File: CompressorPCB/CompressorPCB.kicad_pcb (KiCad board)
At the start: 4 copper layers, 118 parts, among them J1 PowerJack, J2 SWD Header, J3 Header, J5 In, J6 Out, Q1 BC847, Q2 BC857, Q3 BC857, Q4 2N7002, SW2 RST, U1 TL074, U2 TL074, U3 LM13700, U4 LMR62014XMF, U5 AMS1117, U6 NCS20074D, U7 STM32L052K6T6, U8 74HC595, U9 74HC595

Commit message: fixed resistor array footprints
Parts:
- removed RN3, RN4: 470, Resistor_THT:R_Array_SIP8
- added RN5: 470, Resistor_SMD:R_Cat16-4, F.Cu at (209.5, -3.92)
- added RN6: 470, Resistor_SMD:R_Cat16-4, F.Cu at (213.4, -3.92)
- RN1, RN2: footprint Resistor_THT:R_Array_SIP8 -> Resistor_SMD:R_Cat16-4
- moved RN1 75.9 mm to (166.9, -24.8)
- moved U10 71.0 mm to (174.0, -43.9)
- moved RN2 46.7 mm to (205.7, -3.92)
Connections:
- RN1 pad 2: GND -> Net-(RN1B-R2.1)
- RN1 pad 3: Net-(RN1B-R2.1) -> Net-(RN1C-R3.1)
- RN1 pad 4: GND -> Net-(RN1D-R4.1)
- RN1 pad 5: Net-(RN1C-R3.1) -> GND
- RN1 pad 7: Net-(RN1D-R4.1) -> GND
- RN2 pad 2: GND -> Net-(RN2B-R2.1)
- RN2 pad 3: Net-(RN2B-R2.1) -> Net-(RN2C-R3.1)
- RN2 pad 4: GND -> Net-(RN2D-R4.1)
- RN2 pad 5: Net-(RN2C-R3.1) -> GND
- RN2 pad 7: Net-(RN2D-R4.1) -> GND
- U10 pad 10: Net-(RN2A-R1.1) -> Net-(RN1A-R1.1)
- U10 pad 12: Net-(RN2B-R2.1) -> Net-(RN1B-R2.1)
- U10 pad 14: Net-(RN2C-R3.1) -> Net-(RN1C-R3.1)
- U10 pad 16: Net-(RN2D-R4.1) -> Net-(RN1D-R4.1)
- U10 pad 2: Net-(RN1A-R1.1) -> Net-(RN5A-R1.1)
- U10 pad 4: Net-(RN1B-R2.1) -> Net-(RN5B-R2.1)
- U10 pad 6: Net-(RN1C-R3.1) -> Net-(RN5C-R3.1)
- U10 pad 8: Net-(RN1D-R4.1) -> Net-(RN5D-R4.1)
- U11 pad 10: Net-(RN4A-R1.1) -> Net-(RN2A-R1.1)
- U11 pad 12: Net-(RN4B-R2.1) -> Net-(RN2B-R2.1)
- U11 pad 14: Net-(RN4C-R3.1) -> Net-(RN2C-R3.1)
- U11 pad 16: Net-(RN4D-R4.1) -> Net-(RN2D-R4.1)

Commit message: basic layout
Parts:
- C1, C10, C11, C12, C13, C14, C15, C16, C17, C18, C19, C2, C20, C22, C3, C4, C5, C6, C7, C8, C9, D1, D10, D12, D13, D14, D15, D16, D2, D6, D9, J1, J2, J5, J6, J8, L1, Q1, Q2, Q3, Q4, R1, R11, R12, R13, R14, R15, R16, R17, R18, R19, R2, R20, R21, R22, R23, R24, R26, R27, R29, R3, R30, R31, R33, R34, R35, R36, R37, R38, R39, R4, R40, R41, R42, R43, R44, R45, R46, R47, R48, R49, R5, R50, R51, R52, R53, R54, R56, R57, R7, R8, R9, SW2, U1, U2, U3, U4, U5, U6, U7: moved to B.Cu
- moved R28 331.9 mm to (-39.0, 33.2)
- moved R32 315.9 mm to (-4.75, 30.4)
- moved R41 307.9 mm to (-20.4, -2.23), turned to 180 degrees
- moved D15 307.8 mm to (-38.5, 24.1), turned to -90 degrees
- moved SW2 306.8 mm to (-39.6, 15.1), turned to -90 degrees
- moved D14 304.4 mm to (-31.6, 29.3), turned to 180 degrees
- moved J2 300.5 mm to (-40.5, -42.7), turned to 180 degrees
- moved D16 297.4 mm to (-31.6, 15.7)
- moved C15 296.7 mm to (-16.3, -2.23)
- moved D12 290.3 mm to (-23.7, 3.48), turned to 180 degrees
- moved D13 287.7 mm to (-20.8, 7.38), turned to 90 degrees
- moved C1 285.0 mm to (-33.0, 21.8)
- moved U1 284.3 mm to (-27.3, 21.8)
- moved U7 282.9 mm to (-18.7, -17.4), turned to -135 degrees
- moved Q1 282.5 mm to (-9.60, 5.57), turned to 180 degrees
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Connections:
- C2 pad 2: Net-(U1A-+) -> Net-(U1D-+)
- R1 pad 1: Net-(U1A-+) -> Net-(U1D-+)
- R12 pad 2: Net-(U1B--) -> Net-(U1A--)
- R16 pad 1: Net-(U1B--) -> Net-(U1A--)
- R17 pad 1: Net-(U1B--) -> Net-(U1A--)
- R19 pad 2: Net-(U1C--) -> Net-(U1B--)
- R2 pad 1: Net-(U2B--) -> Net-(U2C--)
- R23 pad 1: Net-(U1C--) -> Net-(U1B--)
- R25 pad 2: Net-(U2A-+) -> Net-(U2B-+)
- R29 pad 2: Net-(U2A--) -> Net-(U2B--)
- R3 pad 1: Net-(U2B--) -> Net-(U2C--)
- R31 pad 1: Net-(U2A--) -> Net-(U2B--)
- R4 pad 1: Net-(U1A--) -> Net-(U1D--)
- R44 pad 2: Net-(U6C--) -> Net-(U6D--)
- R46 pad 1: Net-(U6C--) -> Net-(U6D--)
- R49 pad 2: Net-(U6D--) -> Net-(U6C--)
- R5 pad 1: Net-(U1A--) -> Net-(U1D--)
- R50 pad 1: Net-(U6D--) -> Net-(U6C--)
- RN1 pad 1: Net-(RN1A-R1.1) -> GND
- RN1 pad 2: Net-(RN1B-R2.1) -> GND
- RN1 pad 3: Net-(RN1C-R3.1) -> GND
- RN1 pad 4: Net-(RN1D-R4.1) -> GND
- RN1 pad 5: GND -> Net-(RN1D-R4.2)
- RN1 pad 6: GND -> Net-(RN1C-R3.2)
- RN1 pad 7: GND -> Net-(RN1B-R2.2)
- RN1 pad 8: GND -> Net-(RN1A-R1.2)
- RN2 pad 1: Net-(RN2A-R1.1) -> GND
- RN2 pad 2: Net-(RN2B-R2.1) -> GND
- RN2 pad 3: Net-(RN2C-R3.1) -> GND
- RN2 pad 4: Net-(RN2D-R4.1) -> GND
- RN2 pad 5: GND -> Net-(RN2D-R4.2)
- RN2 pad 6: GND -> Net-(RN2C-R3.2)
- RN2 pad 7: GND -> Net-(RN2B-R2.2)
- RN2 pad 8: GND -> Net-(RN2A-R1.2)
- RN5 pad 1: Net-(RN5A-R1.1) -> GND
- RN5 pad 2: Net-(RN5B-R2.1) -> GND
- RN5 pad 3: Net-(RN5C-R3.1) -> GND
- RN5 pad 4: Net-(RN5D-R4.1) -> GND
- RN5 pad 5: GND -> Net-(RN5D-R4.2)
- RN5 pad 6: GND -> Net-(RN5C-R3.2)
- RN5 pad 7: GND -> Net-(RN5B-R2.2)
- RN5 pad 8: GND -> Net-(RN5A-R1.2)
- RN6 pad 1: Net-(RN6A-R1.1) -> GND
- RN6 pad 2: Net-(RN6B-R2.1) -> GND
- RN6 pad 3: Net-(RN6C-R3.1) -> GND
- RN6 pad 4: Net-(RN6D-R4.1) -> GND
- RN6 pad 5: GND -> Net-(RN6D-R4.2)
- RN6 pad 6: GND -> Net-(RN6C-R3.2)
- RN6 pad 7: GND -> Net-(RN6B-R2.2)
- RN6 pad 8: GND -> Net-(RN6A-R1.2)
- U1 pad 1: /Analog/InAmp -> Net-(D14-K)
- U1 pad 10: /Analog/Dcathode -> /Analog/EnvCap
- U1 pad 12: /Analog/EnvCap -> Net-(U1D-+)
- U1 pad 13: ENV -> Net-(U1D--)
- U1 pad 14: ENV -> /Analog/InAmp
- U1 pad 3: Net-(U1A-+) -> +9VA
- U1 pad 5: +9VA -> /Analog/Dcathode
- U1 pad 7: Net-(D14-K) -> Net-(D16-A)
- U1 pad 8: Net-(D16-A) -> ENV
- U1 pad 9: Net-(U1C--) -> ENV
- U10 pad 10: Net-(RN1A-R1.1) -> Net-(RN1A-R1.2)
- U10 pad 12: Net-(RN1B-R2.1) -> Net-(RN1B-R2.2)
- U10 pad 14: Net-(RN1C-R3.1) -> Net-(RN1C-R3.2)
- U10 pad 16: Net-(RN1D-R4.1) -> Net-(RN1D-R4.2)
- U10 pad 2: Net-(RN5A-R1.1) -> Net-(RN5A-R1.2)
- U10 pad 4: Net-(RN5B-R2.1) -> Net-(RN5B-R2.2)
- U10 pad 6: Net-(RN5C-R3.1) -> Net-(RN5C-R3.2)
- U10 pad 8: Net-(RN5D-R4.1) -> Net-(RN5D-R4.2)
- U11 pad 10: Net-(RN2A-R1.1) -> Net-(RN2A-R1.2)
- U11 pad 12: Net-(RN2B-R2.1) -> Net-(RN2B-R2.2)
- U11 pad 14: Net-(RN2C-R3.1) -> Net-(RN2C-R3.2)
- U11 pad 16: Net-(RN2D-R4.1) -> Net-(RN2D-R4.2)
- U11 pad 2: Net-(RN6A-R1.1) -> Net-(RN6A-R1.2)
- U11 pad 4: Net-(RN6B-R2.1) -> Net-(RN6B-R2.2)
- U11 pad 6: Net-(RN6C-R3.1) -> Net-(RN6C-R3.2)
- U11 pad 8: Net-(RN6D-R4.1) -> Net-(RN6D-R4.2)
- U2 pad 1: Net-(C7-Pad1) -> Net-(Q1-B)
- U2 pad 10: Vamp -> ENV
- U2 pad 2: Net-(U2A--) -> Net-(Q1-E)
- U2 pad 3: Net-(U2A-+) -> Vamp
- U2 pad 5: ENV -> Net-(U2B-+)
- U2 pad 7: /Analog/RatioAmp -> Net-(C7-Pad1)
- U2 pad 8: Net-(Q1-B) -> /Analog/RatioAmp
- U2 pad 9: Net-(Q1-E) -> Net-(U2C--)
- U6 pad 14: Net-(R50-Pad2) -> Net-(R46-Pad2)
- U6 pad 8: Net-(R46-Pad2) -> Net-(R50-Pad2)
- U7 pad 10: /Digital/LED_Latch -> unconnected-(U7-PA4-Pad10)
- U7 pad 11: /Digital/LED_SCK -> unconnected-(U7-PA5-Pad11)
- U7 pad 13: /Digital/LED_MOSI -> unconnected-(U7-PA7-Pad13)
- U7 pad 14: /Digital/LED_NRST -> unconnected-(U7-PB0-Pad14)
- U7 pad 20: unconnected-(U7-PA10-Pad20) -> /Digital/BYP_LED
- U7 pad 25: unconnected-(U7-PA15-Pad25) -> /Digital/LED_Latch
- U7 pad 26: /Digital/BYP_LED -> /Digital/LED_SCK
- U7 pad 28: unconnected-(U7-PB5-Pad28) -> /Digital/LED_MOSI
- U7 pad 29: unconnected-(U7-PB6-Pad29) -> /Digital/LED_NRST
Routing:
- added copper zone on B.Cu, net GND
- added copper zone on F.Cu, net GND
- added copper zone on In1.Cu, net GND
- added copper zone on In2.Cu, net GND

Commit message: routing start
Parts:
- moved R48 3.40 mm to (-11.7, -7.72)
- moved C16 2.13 mm to (-8.32, -7.65)
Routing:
- net +3.3V: track 0.00 -> 233.3 mm, vias 0 -> 3
- net +9VA: track 0.00 -> 170.5 mm, vias 0 -> 3
- net +18V: track 0.00 -> 152.5 mm, vias 0 -> 8
- net NRST: track 0.00 -> 84.9 mm, vias 0 -> 1
- net /Digital/LED_NRST: track 0.00 -> 84.9 mm, vias 0 -> 2
- net /Digital/LED_Latch: track 0.00 -> 77.3 mm, vias 0 -> 2
- net /Digital/LED_SCK: track 0.00 -> 65.8 mm, vias 0 -> 2
- net Net-(U8-QH'): track 0.00 -> 62.4 mm, vias 0 -> 2
- net VCC: track 0.00 -> 51.3 mm
- net Net-(U8-QA): track 0.00 -> 34.4 mm
- net +3.3VA: track 0.00 -> 34.3 mm, vias 0 -> 1
- net SWCLK: track 0.00 -> 31.6 mm
- net SWDIO: track 0.00 -> 28.6 mm
- net /Digital/Output_ADC: track 0.00 -> 24.2 mm, vias 0 -> 2
- net Net-(U8-QB): track 0.00 -> 23.0 mm
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
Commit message: all routed, no DRC
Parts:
- moved R56 10.6 mm to (-11.9, -13.4)
- moved C20 0.17 mm to (-20.6, -7.52)
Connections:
- J3 pad 1: /Digital/InJack -> /Digital/OutJack
- J3 pad 2: FX_IN -> FX_OUT
- J3 pad 3: /Digital/OutJack -> /Digital/InJack
- J3 pad 4: FX_OUT -> FX_IN
- U7 pad 18: BYP_IN -> unconnected-(U7-PA8-Pad18)
- U7 pad 9: unconnected-(U7-PA3-Pad9) -> BYP_IN
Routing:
- net /Digital/OutJack: track 0.00 -> 96.8 mm, vias 0 -> 1
- net BYP_IN: track 2.09 -> 88.0 mm, vias 0 -> 2
- net OUT_BIASED: track 0.00 -> 84.5 mm, vias 0 -> 2
- net Net-(U2B-+): track 0.00 -> 76.6 mm, vias 0 -> 2
- net /Digital/InJack: track 0.00 -> 76.0 mm
- net Net-(D13-K): track 0.00 -> 75.9 mm, vias 0 -> 2
- net ENV: track 1.27 -> 65.7 mm, vias 0 -> 2
- net FX_IN: track 0.00 -> 45.9 mm
- net /Digital/BYP_LED: track 0.00 -> 41.0 mm, vias 0 -> 2
- net Net-(R46-Pad2): track 4.23 -> 44.5 mm, vias 0 -> 2
- net /Analog/EnvCap: track 0.00 -> 40.3 mm, vias 0 -> 1
- net FX_OUT: track 0.00 -> 38.7 mm, vias 0 -> 1
- net /Analog/RatioAmp: track 0.00 -> 32.3 mm, vias 0 -> 2
- net /Digital/LED_SCK: track 65.8 -> 97.5 mm, vias 2 -> 3
- net /Analog/InAmp: track 0.00 -> 28.6 mm, vias 0 -> 2
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
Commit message: niceties
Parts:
- moved SW2 35.9 mm to (-39.1, -20.8)
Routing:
- net NRST: track 84.9 -> 47.3 mm
- net SWCLK: track 31.6 -> 34.3 mm
- net /Digital/OutJack: track 96.8 -> 99.2 mm
- net SWDIO: track 28.6 -> 30.9 mm
- net /Digital/LED_SCK: track 97.5 -> 99.4 mm
- net /Digital/LED_Latch: track 102.4 -> 103.9 mm
- net /Analog/FullRect: track 25.9 -> 24.4 mm
- net /Digital/LED_MOSI: track 24.4 -> 25.5 mm
- net Net-(U9-QA): track 20.7 -> 19.5 mm
- net Net-(U8-QB): track 23.0 -> 21.9 mm
- net Net-(RN1D-R4.2): track 5.21 -> 6.09 mm
- net Net-(R18-Pad1): track 16.3 -> 15.6 mm
- net GND: vias 52 -> 77

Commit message: routing start
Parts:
- removed D14, D15, D2: 1N4148W, Diode_SMD:D_SOD-123
- removed R23, R42: 100k, Resistor_SMD:R_0805_2012Metric
- removed R27, R30: 1k, Resistor_SMD:R_0805_2012Metric
- removed R47: 680k, Resistor_SMD:R_0805_2012Metric
- added C24: 22n, Capacitor_SMD:C_0805_2012Metric, B.Cu at (12.1, -12.7)
- added R58: 220, Resistor_SMD:R_0805_2012Metric, B.Cu at (0.77, -0.42)
- added R59: 100k, Resistor_SMD:R_0805_2012Metric, B.Cu at (-9.76, -5.93)
- added R60: 47k, Resistor_SMD:R_0805_2012Metric, B.Cu at (7.78, -2.33)
- added R61: 22k, Resistor_SMD:R_0805_2012Metric, B.Cu at (5.28, 0.72)
- C16: value 1u -> 470n
- R12: value 100k -> 10k
- R16: value 100k -> 1k
- R19: value 100k -> 220
- R43: value 47k -> 91k
- R44: value 56k -> 47k
- R45: value 22k -> 47k
- R48: value 10k -> 1k
- moved R16 33.9 mm to (-3.91, 34.8), turned to 0 degrees
- moved R12 30.2 mm to (2.76, 33.1)
- moved R44 17.0 mm to (-5.68, -9.47), turned to -90 degrees
- moved R49 14.1 mm to (15.9, -12.4), turned to 90 degrees
- moved D16 12.8 mm to (-35.0, 28.0)
- moved C18 12.6 mm to (8.41, -6.31), turned to 0 degrees
- moved R2 11.9 mm to (-13.0, 20.2)
- moved R46 11.9 mm to (-2.19, -9.62), turned to 90 degrees
- moved R48 7.57 mm to (-6.36, -2.37), turned to -90 degrees
- moved R17 7.47 mm to (-36.2, 20.7), turned to 90 degrees
- moved R54 7.12 mm to (0.33, -17.6)
- moved R43 6.82 mm to (9.76, -9.15), turned to 90 degrees
- moved R19 5.82 mm to (-38.0, 24.0), turned to 0 degrees
- moved C16 5.48 mm to (-9.77, -2.36), turned to 90 degrees
- moved R1 3.90 mm to (-18.1, 24.2)
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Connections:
- D16 pad 1: /Analog/FullRect -> Net-(D16-K)
- R12 pad 1: /Analog/InAmp -> Net-(R12-Pad1)
- R12 pad 2: Net-(U1A--) -> Net-(U1C-+)
- R16 pad 1: Net-(U1A--) -> ENV
- R16 pad 2: /Analog/Dcathode -> Net-(R12-Pad1)
- R17 pad 1: Net-(U1A--) -> /Analog/EnvCap
- R17 pad 2: /Analog/Danode -> Net-(U1C--)
- R19 pad 1: /Analog/Danode -> Net-(D16-K)
- R19 pad 2: Net-(U1B--) -> Net-(U1A--)
- R28 pad 1: Net-(R27-Pad2) -> Net-(U1A--)
- R32 pad 2: Net-(R30-Pad2) -> Net-(U1C-+)
- R32 pad 3: Net-(R30-Pad2) -> Net-(R12-Pad1)
- R49 pad 1: Net-(U6B--) -> Net-(R49-Pad1)
- R49 pad 2: Net-(U6C--) -> Net-(U6A--)
- R50 pad 1: Net-(U6C--) -> Net-(U6A--)
- R50 pad 2: Net-(R50-Pad2) -> Net-(C24-Pad2)
- R54 pad 1: Net-(R50-Pad2) -> Net-(C24-Pad2)
- U1 pad 1: Net-(D14-K) -> Net-(D16-A)
- U1 pad 10: /Analog/EnvCap -> Net-(U1C-+)
- U1 pad 3: +9VA -> /Analog/InAmp
- U1 pad 5: /Analog/Dcathode -> /Analog/EnvCap
- U1 pad 6: Net-(U1B--) -> ENV
- U1 pad 7: Net-(D16-A) -> ENV
- U1 pad 8: ENV -> Net-(U1C--)
- U1 pad 9: ENV -> Net-(U1C--)
- U2 pad 10: ENV -> unconnected-(U2C-+-Pad10)
- U6 pad 1: Net-(D1-A) -> Net-(C24-Pad2)
- U6 pad 10: /Digital/vMirror -> OUT_BIASED
- U6 pad 2: Net-(D2-A) -> Net-(U6A--)
- U6 pad 3: +9VA -> /Digital/vMirror
- U6 pad 7: Net-(U6B--) -> Net-(R49-Pad1)
- U6 pad 8: Net-(R50-Pad2) -> Net-(R58-Pad1)
- U6 pad 9: Net-(U6C--) -> /Digital/Rect
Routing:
- net +3.3V: track 248.6 -> 39.0 mm, vias 3 -> 0
- net /Digital/OutJack: track 99.2 -> 0.00 mm, vias 1 -> 0
- net OUT_BIASED: track 84.5 -> 0.00 mm, vias 2 -> 0
- net BYP_IN: track 88.0 -> 3.55 mm, vias 2 -> 0
- net /Digital/LED_NRST: track 107.8 -> 30.4 mm, vias 2 -> 1
- net Net-(U2B-+): track 76.6 -> 0.00 mm, vias 2 -> 0
- net /Digital/InJack: track 76.0 -> 0.00 mm
- net Net-(D13-K): track 75.9 -> 0.00 mm, vias 2 -> 0
- net /Digital/LED_Latch: track 103.9 -> 29.8 mm, vias 3 -> 1
- net /Digital/LED_SCK: track 99.4 -> 27.2 mm, vias 3 -> 1
- net FX_IN: track 45.9 -> 0.00 mm
- net /Digital/BYP_LED: track 41.0 -> 0.00 mm, vias 2 -> 0
- net FX_OUT: track 38.7 -> 0.00 mm, vias 1 -> 0
- net Net-(R46-Pad2): track 44.5 -> 8.76 mm, vias 2 -> 0
- net NRST: track 47.3 -> 14.3 mm, vias 1 -> 0
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
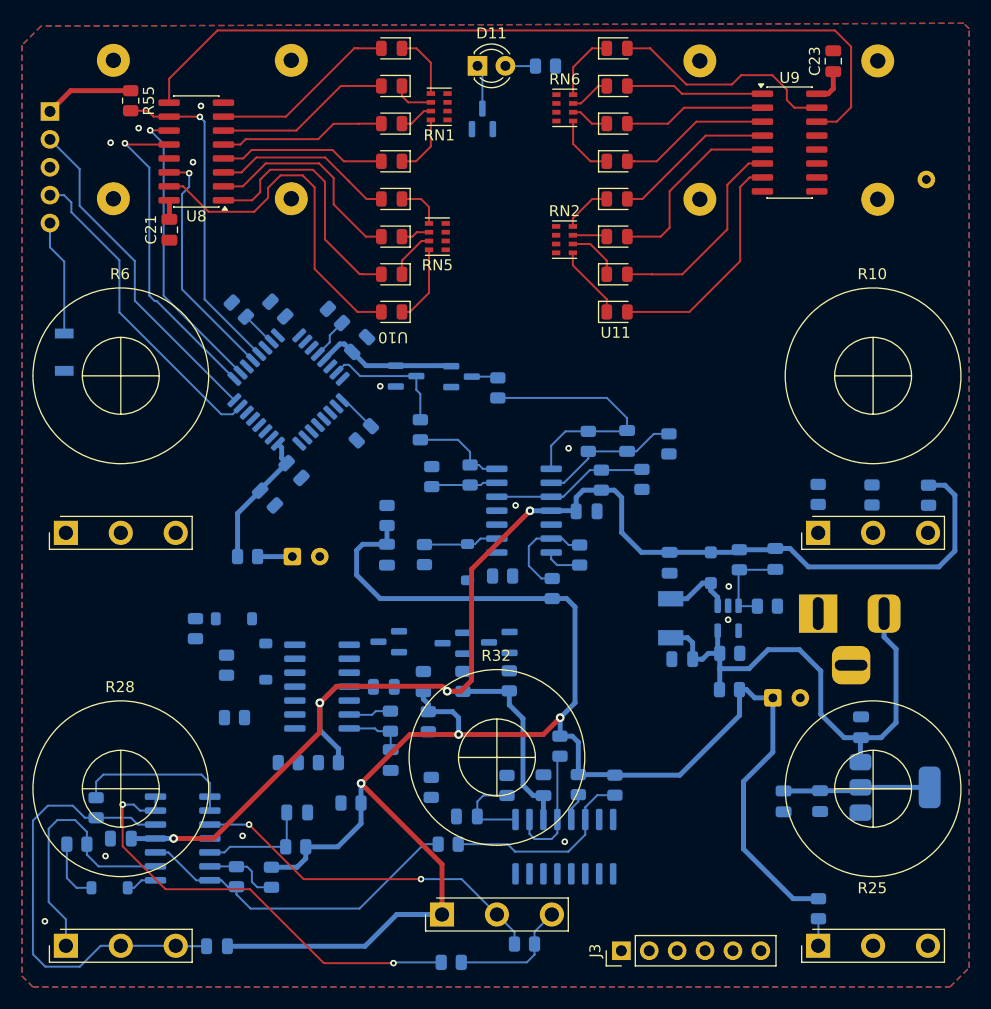
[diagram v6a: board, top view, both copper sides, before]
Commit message: all routed, DRC passing
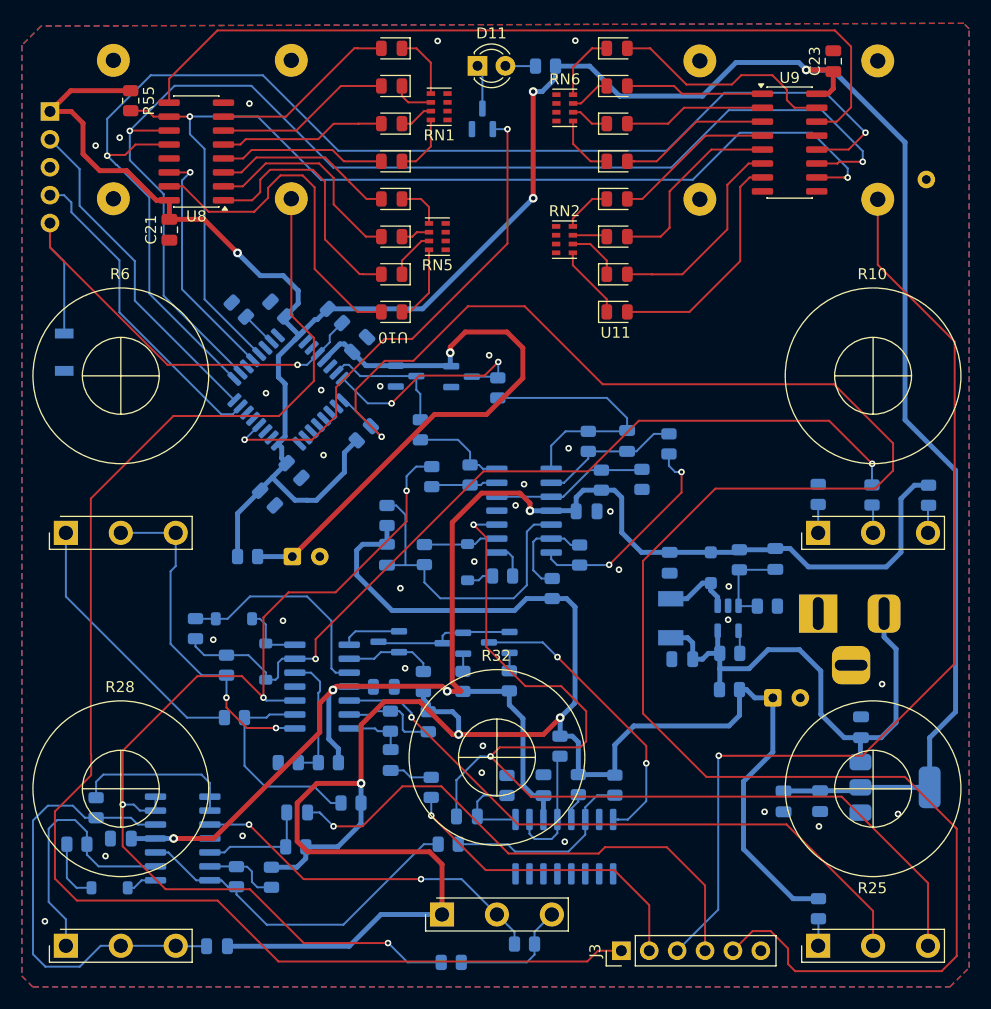
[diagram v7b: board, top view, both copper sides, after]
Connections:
- U2 pad 10: unconnected-(U2C-+-Pad10) -> ENV
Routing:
- net +3.3V: track 39.0 -> 238.6 mm, vias 0 -> 4
- net BYP_IN: track 3.55 -> 178.5 mm, vias 0 -> 1
- net /Digital/OutJack: track 0.00 -> 133.3 mm
- net OUT_BIASED: track 0.00 -> 94.9 mm, vias 0 -> 2
- net /Digital/InJack: track 0.00 -> 89.5 mm, vias 0 -> 1
- net /Digital/LED_Latch: track 29.8 -> 116.9 mm, vias 1 -> 2
- net /Digital/LED_SCK: track 27.2 -> 110.3 mm, vias 1 -> 2
- net Net-(D13-K): track 0.00 -> 79.1 mm, vias 0 -> 2
- net /Digital/LED_NRST: track 30.4 -> 98.9 mm, vias 1 -> 2
- net Net-(U2B-+): track 0.00 -> 59.1 mm, vias 0 -> 1
- net ENV: track 41.7 -> 96.7 mm, vias 2 -> 4
- net FX_IN: track 0.00 -> 48.4 mm, vias 0 -> 1
- net /Digital/BYP_LED: track 0.00 -> 46.5 mm, vias 0 -> 2
- net +3.3VA: track 16.2 -> 56.2 mm, vias 0 -> 1
- net /Analog/RatioAmp: track 0.00 -> 31.6 mm, vias 0 -> 2
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
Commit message: elbow room, stitching vias
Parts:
- moved R12 1.35 mm to (2.77, 34.4)
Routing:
- net +3.3VA: track 56.2 -> 42.0 mm
- net Net-(R49-Pad1): track 19.8 -> 24.6 mm
- net /Digital/Output_ADC: track 20.5 -> 25.1 mm, vias 2 -> 0
- net BYP_IN: track 178.5 -> 182.9 mm
- net Net-(R46-Pad2): track 8.76 -> 12.8 mm, vias 0 -> 2
- net +3.3V: track 238.6 -> 236.6 mm
- net Net-(R12-Pad1): track 11.3 -> 13.1 mm
- net Net-(U1C-+): track 32.9 -> 34.2 mm
- net ENV: track 96.7 -> 97.3 mm
- net GND: vias 32 -> 64
